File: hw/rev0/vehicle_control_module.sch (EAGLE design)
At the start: 455 parts, among them IC1 SJA1105TELY, IC10 TJA1100HNZ, IC11 KSZ8061MNXI-TR, IC12 TJA1100HNZ, IC14 NUP2202W1T2G, IC15 TLE9252VSKXUMA1, IC16 NUP2202W1T2G, IC17 LP5907QMFX-3.3Q1, IC2 ATSAMV71Q21B-AABT, IC3 TJA1100HNZ, IC4 FT2232HL, IC5 TRS3232EQPWRQ1, IC6 SST26VF032BT-104I_SM, IC7 DS3231SN#, IC8 TLE9252VSKXUMA1, IC9 TPS62242DRVR, J10 5-2337992-3, J11 2301843-1, J12 1017505, J13 2301843-1, J15 693022010811, J2 2305018-2, J27 2041119-2, J3 1017505, J4 1017505, J5 1017505, J6 1017505, J7 1017505, J8 1017505, J9 1017505, U1 122-2920-GR, U2 LM63625, U3 TPS62007-Q1_DGS_10, Y1 NX3225SA-25MHZ-EXS00A-CS11338, Y2 NX2016SA-25.000M-STD-CZS-1, Y3 ABM8AIG-12.000MHZ-1Z-T

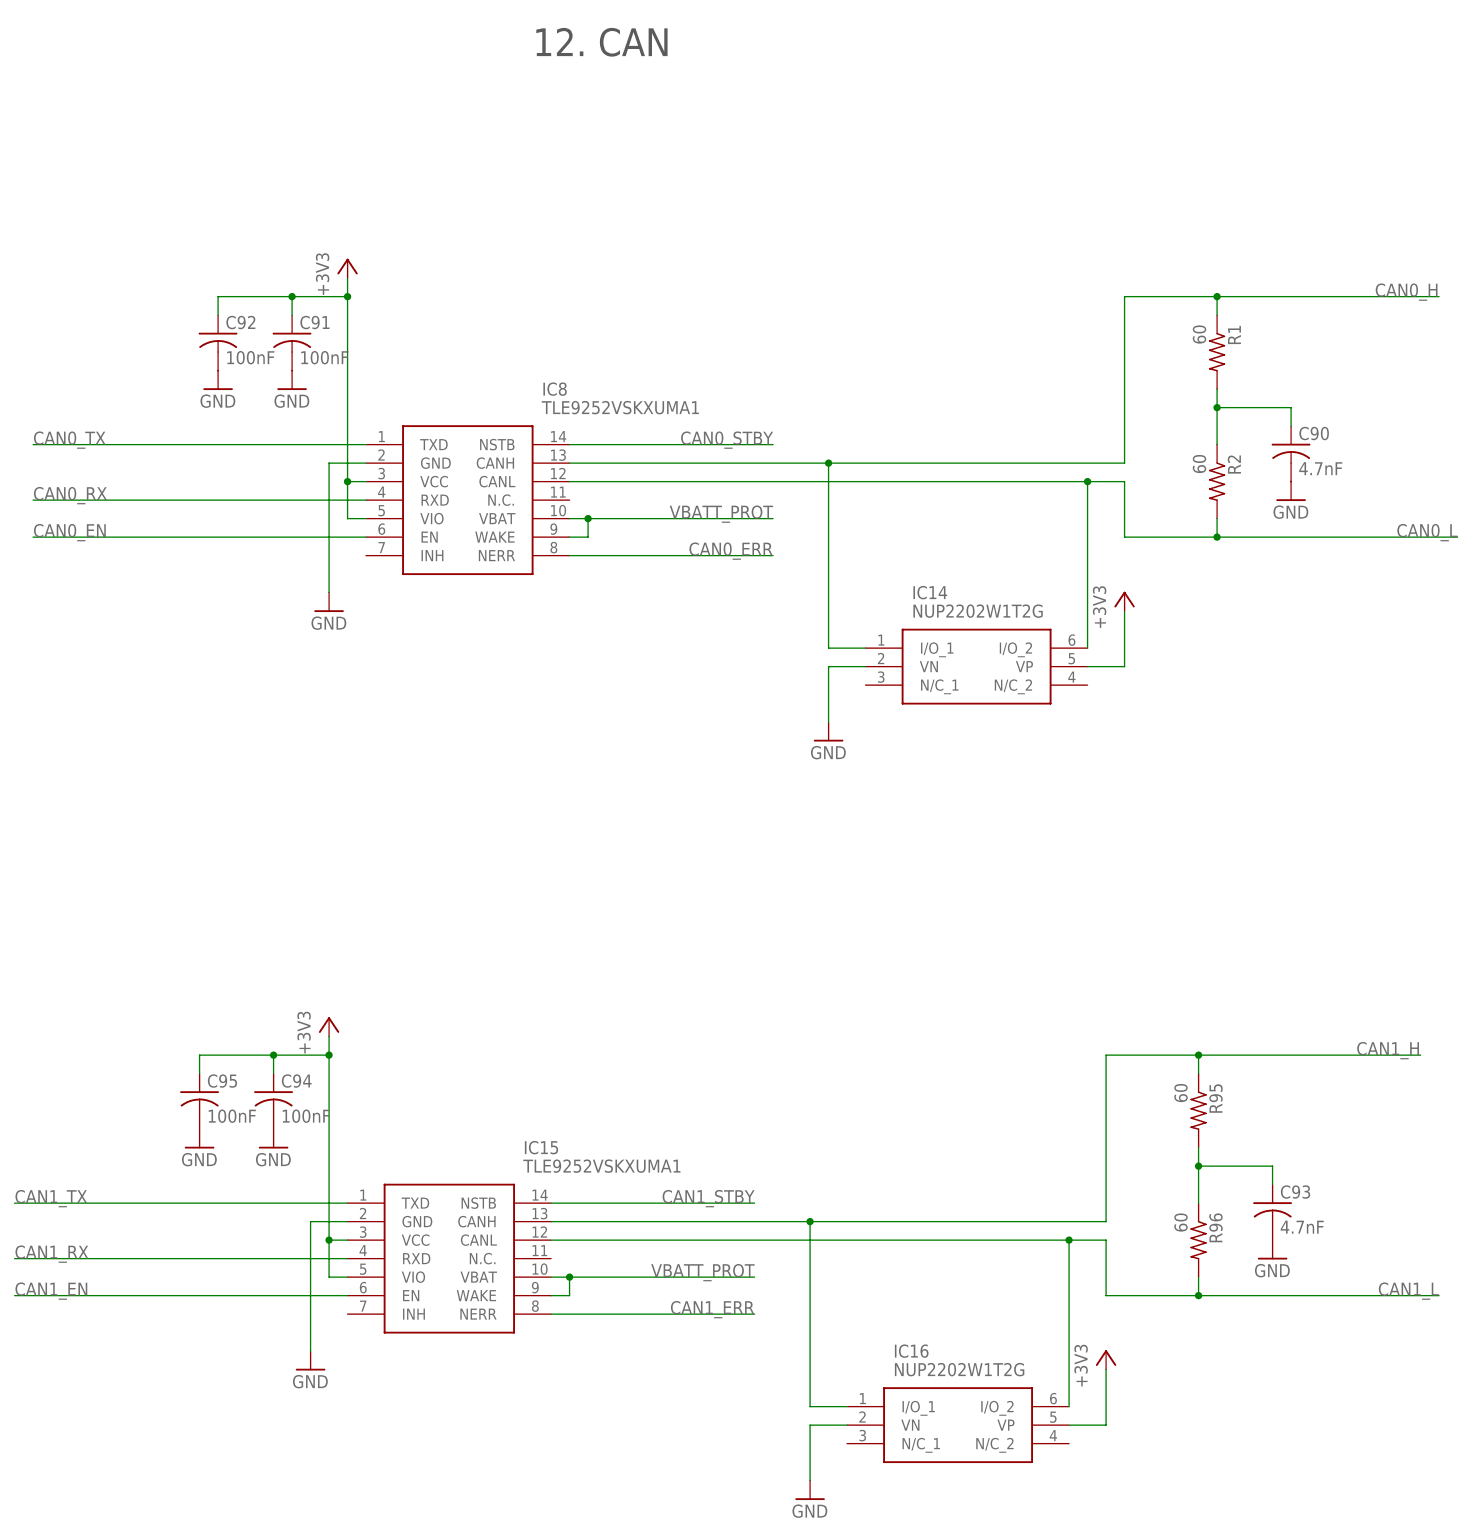
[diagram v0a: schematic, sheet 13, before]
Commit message: Swap to simple CAN transciever, no wake on CAN functionality required
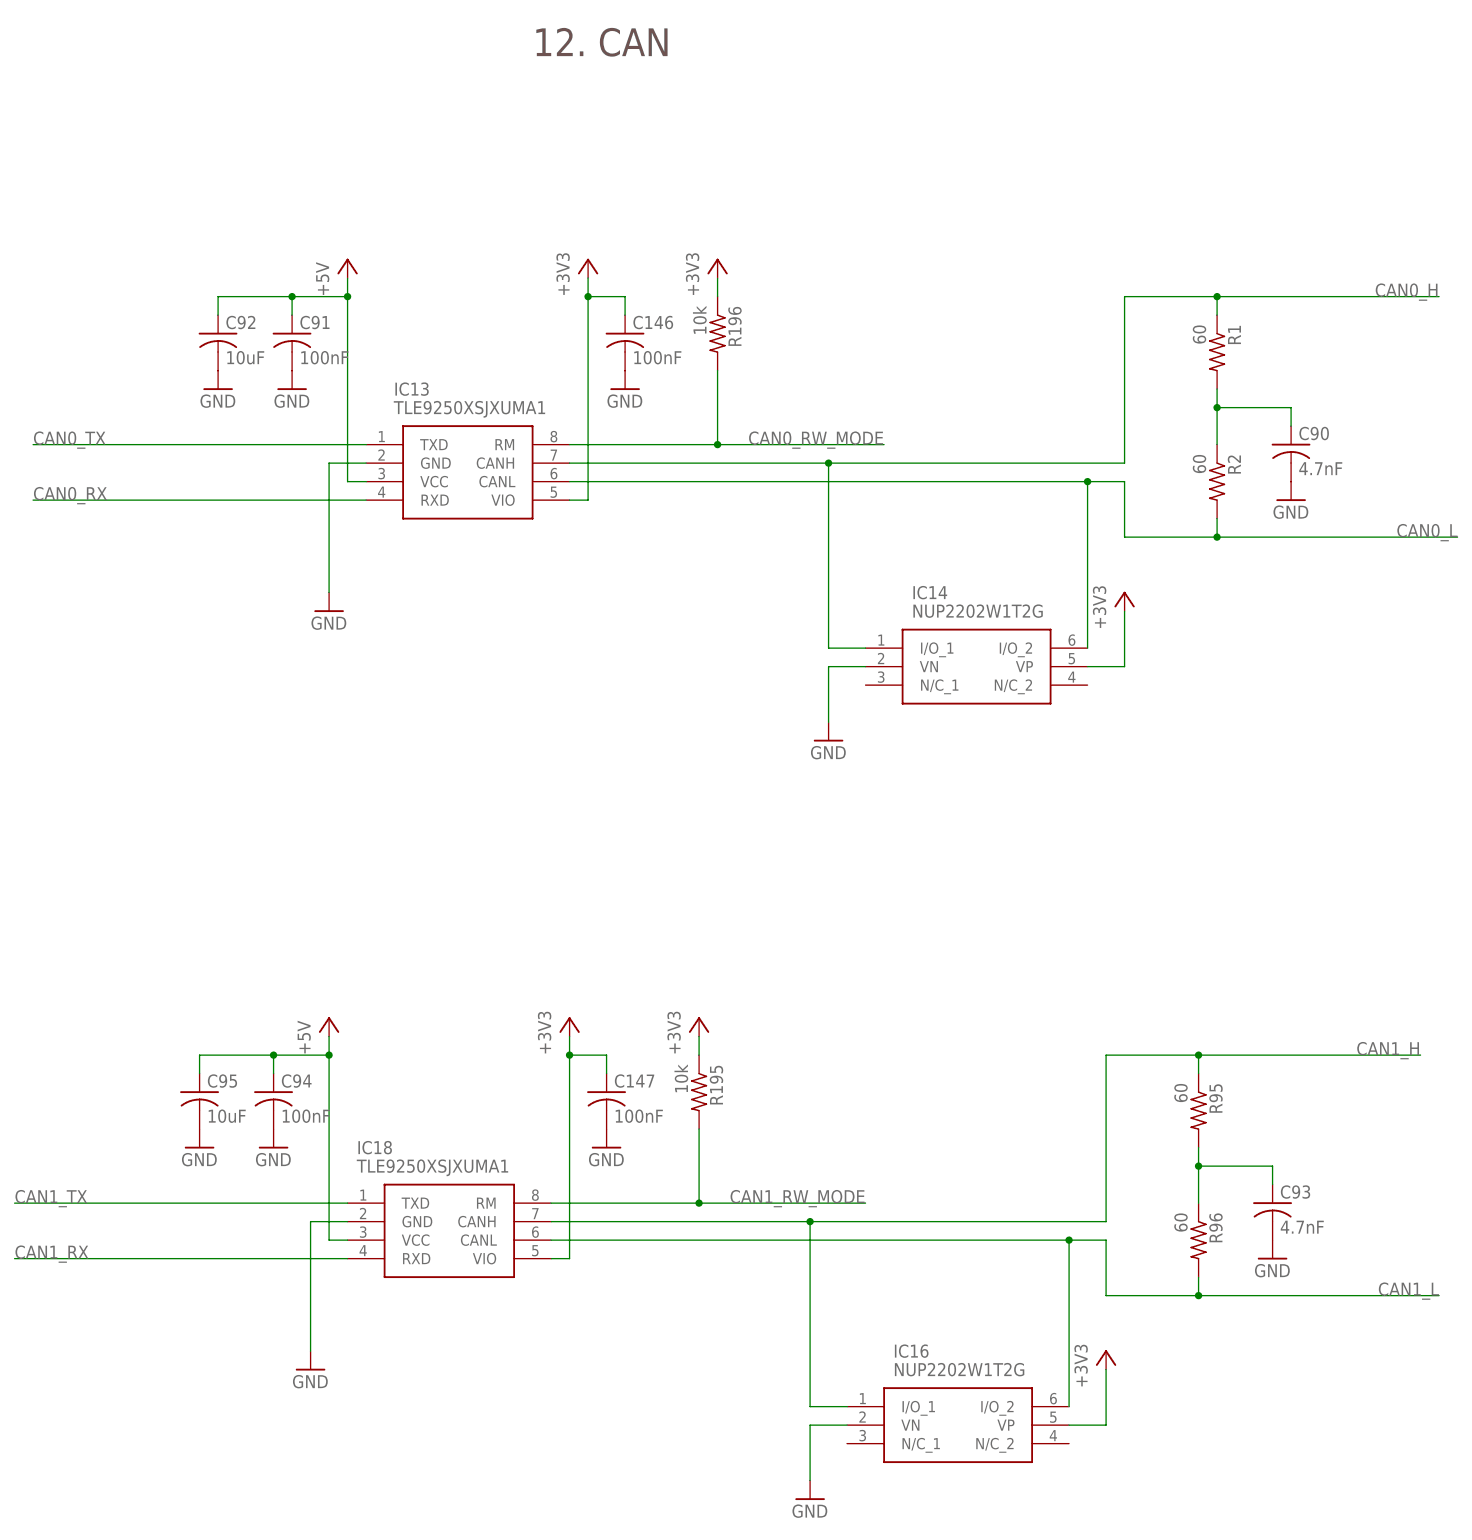
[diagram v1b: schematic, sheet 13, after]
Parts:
- removed IC15, IC8: TLE9252VSKXUMA1, samacsys:TLE9252VSKXUMA1
- added C146, C147: 100nF, rcl:C-USC0603
- added IC13, IC18: TLE9250XSJXUMA1, samacsys:TLE9250XSJXUMA1
- added R195, R196: 10k, rcl:R-US_R0603
- C92, C95: value 100nF -> 10uF
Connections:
- removed net CAN0_EN: IC2.PA22, IC8.EN
- removed net CAN0_ERR: IC2.PC2, IC8.NERR
- removed net CAN0_STBY: IC2.PC1, IC8.NSTB
- removed net CAN1_EN: IC15.EN, IC2.PC11
- removed net CAN1_ERR: IC15.NERR, IC2.PC10
- removed net CAN1_STBY: IC15.NSTB, IC2.PA2
- new net CAN0_RW_MODE: IC13.RM, IC2.PA7, R196.2
- new net CAN1_RW_MODE: IC18.RM, IC2.PA2, R195.2
- net +3V3: now also C146.1, C147.1, IC13.VIO, IC18.VIO, R195.1, R196.1; no longer C91.1, C92.1, C94.1, C95.1, IC15.VCC, IC15.VIO, IC8.VCC, IC8.VIO
- net +5V: now also C91.1, C92.1, C94.1, C95.1, IC13.VCC, IC18.VCC
- net CAN0_H: now also IC13.CANH; no longer IC8.CANH
- net CAN0_L: now also IC13.CANL; no longer IC8.CANL
- net CAN0_RX: now also IC13.RXD; no longer IC8.RXD
- net CAN0_TX: now also IC13.TXD; no longer IC8.TXD
- net CAN1_H: now also IC18.CANH; no longer IC15.CANH
- net CAN1_L: now also IC18.CANL; no longer IC15.CANL
- net CAN1_RX: now also IC18.RXD; no longer IC15.RXD
- net CAN1_TX: now also IC18.TXD; no longer IC15.TXD
- net GND: now also C146.2, C147.2, IC13.GND, IC18.GND; no longer IC15.GND, IC8.GND
- net VBATT_PROT: no longer IC15.VBAT, IC15.WAKE, IC8.VBAT, IC8.WAKE

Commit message: Add digital inputs, connect MCU power supply
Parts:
- removed C30, C31: 8pF, rcl:C-USC0603
- removed IC14, IC16: NUP2202W1T2G, samacsys:NUP2202W1T2G
- removed R183, R188, R193: 1k, rcl:R-US_R0603
- removed Y2: NX2016SA-25.000M-STD-CZS-1, samacsys:NX2016SA-25.000M-STD-CZS-1
- added C148, C149, C150, C151, C152, C153, C154, C155: 0.01uF, rcl:C-USC0603
- added C156, C157, C158, C159, C160, C161, C163, C164, C166, C167, C168, C169, C170, C171, C172: 100nF, rcl:C-USC0603
- added C162: 1uF, rcl:C-USC0603
- added C165: 4.7uF, rcl:C-USC0603
- added D28, D29, D30, D31, D32, D33, D34, D35: BAT54SWFILMY, samacsys:BAT54SWFILMY
- added IC8: 74HC7541D-Q100J, samacsys:74HC7541D-Q100J
- added R198: 4.7k, rcl:R-US_R0603
- R109, R118, R128, R138, R148, R158, R168, R178: value 1k -> 100k
- R113, R123, R133, R143, R153, R163, R173: value 1k -> 4.7k
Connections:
- removed net N$22: C31.1, IC11.XI, Y2.CRYSTAL_2
- removed net N$23: C30.1, IC11.XO, Y2.CRYSTAL_1
- new net EXT_DINPUT_0: R198.1
- new net EXT_DINPUT_1: R113.1
- new net EXT_DINPUT_2: R123.1
- new net EXT_DINPUT_3: R133.1
- new net EXT_DINPUT_4: R143.1
- new net EXT_DINPUT_5: R153.1
- new net EXT_DINPUT_6: R163.1
- new net EXT_DINPUT_7: R173.1
- new net INTREG_1V2: C156.1, C157.1, C158.1, C159.1, C160.1, C161.1, C162.1, C163.1, C164.1, IC2.VDDCORE_1, IC2.VDDCORE_2, IC2.VDDCORE_3, IC2.VDDCORE_4, IC2.VDDCORE_5, IC2.VDDOUT, IC2.VDDPLL, IC2.VDDUTMIC
- new net N$148: C148.1, D29.A,K, IC8.A1, R113.2, R118.2
- new net N$149: C149.1, D30.A,K, IC8.A2, R123.2, R128.2
- new net N$150: C150.1, D31.A,K, IC8.A3, R133.2, R138.2
- new net N$151: C151.1, D28.A,K, IC8.A0, R109.2, R198.2
- new net N$152: C152.1, D32.A,K, IC8.A4, R143.2, R148.2
- new net N$153: C153.1, D33.A,K, IC8.A5, R153.2, R158.2
- new net N$154: C154.1, D34.A,K, IC8.A6, R163.2, R168.2
- new net N$155: C155.1, D35.A,K, IC8.A7, R173.2, R178.2
- new net PROT_DINPUT_0: IC2.PD29, IC8.Y0
- new net PROT_DINPUT_1: IC2.PD15, IC8.Y1
- new net PROT_DINPUT_2: IC2.PC17, IC8.Y2
- new net PROT_DINPUT_3: IC2.PD10, IC8.Y3
- new net PROT_DINPUT_4: IC2.PC16, IC8.Y4
- new net PROT_DINPUT_5: IC2.PA1, IC8.Y5
- new net PROT_DINPUT_6: IC2.PC14, IC8.Y6
- new net PROT_DINPUT_7: IC2.PC11, IC8.Y7
- new net SWITCH_REF_CLK: IC1.CLK_OUT, IC11.XI
- net +3V3: now also C165.1, C166.1, C167.1, C168.1, C169.1, C170.1, C171.1, C172.1, D28.A, D29.A, D30.A, D31.A, D32.A, D33.A, D34.A, D35.A, IC1.VDDIO_CLO, IC1.VDDIO_HOST, IC1.VDDIO_MII0_1, IC1.VDDIO_MII0_2, IC1.VDDIO_MII0_3, IC1.VDDIO_MII1_1, IC1.VDDIO_MII1_2, IC1.VDDIO_MII1_3, IC1.VDDIO_MII2_1, IC1.VDDIO_MII2_2, IC1.VDDIO_MII2_3, IC1.VDDIO_MII3_1, IC1.VDDIO_MII3_3, IC1.VDDIO_MII4_1, IC1.VDDIO_MII4_2, IC1.VDDIO_MII4_3, IC2.VDDIN, IC2.VDDIO_1, IC2.VDDIO_2, IC2.VDDIO_3, IC2.VDDIO_4, IC2.VDDIO_5, IC2.VDDPLL_USB, IC2.VDDUTMII, IC8.VCC; no longer IC14.VP, IC16.VP
- net 3V3_AD_REF: now also IC2.VREFP
- net CAN0_H: no longer IC14.I/O_1
- net CAN0_L: no longer IC14.I/O_2
- net CAN0_RW_MODE: now also IC2.PA22; no longer IC2.PA7
- net CAN1_H: no longer IC16.I/O_1
- net CAN1_L: no longer IC16.I/O_2
- net CAN1_RW_MODE: now also IC2.PC10; no longer IC2.PA2
- net GND: now also C148.2, C149.2, C150.2, C151.2, C152.2, C153.2, C154.2, C155.2, C156.2, C157.2, C158.2, C159.2, C160.2, C161.2, C162.2, C163.2, C164.2, C165.2, C166.2, C167.2, C168.2, C169.2, C170.2, C171.2, C172.2, D28.K, D29.K, D30.K, D31.K, D32.K, D33.K, D34.K, D35.K, IC1.VSSA_OSC, IC1.VSSA_PLL, IC1.VSS_43, IC1.VSS_44, IC2.VREFN, IC8.!OE1, IC8.!OE2, IC8.GND, R109.1, R118.1, R128.1, R138.1, R148.1, R158.1, R168.1, R178.1; no longer C112.2, C113.2, C115.2, C117.2, C119.2, C121.2, C123.2, C125.2, C127.2, C129.2, C131.2, C133.2, C135.2, C137.2, C139.2, C141.2, C143.2, C145.2, C30.2, C31.2, IC14.VN, IC16.VN, R109.2, R113.2, R118.2, R123.2, R128.2, R133.2, R138.2, R143.2, R148.2, R153.2, R158.2, R163.2, R168.2, R173.2, R178.2, R183.2, R188.2, R193.2, Y2.GND_1, Y2.GND_2
- net HIGHSIDE_0_EN: now also IC2.PD11
- net HIGHSIDE_10_EN: now also IC2.PC2
- net HIGHSIDE_11_EN: now also IC2.PC3
- net HIGHSIDE_12_EN: now also IC2.PA16
- net HIGHSIDE_13_EN: now also IC2.PD27
- net HIGHSIDE_14_EN: now also IC2.PC7
- net HIGHSIDE_15_EN: now also IC2.PA15
- net HIGHSIDE_16_EN: now also IC2.PC6
- net HIGHSIDE_17_EN: now also IC2.PD24
- net HIGHSIDE_1_EN: now also IC2.PA2
- net HIGHSIDE_2_EN: now also IC2.PA25
- net HIGHSIDE_3_EN: now also IC2.PA7
- net HIGHSIDE_4_EN: now also IC2.PA31
- net HIGHSIDE_5_EN: now also IC2.PA8
- net HIGHSIDE_6_EN: now also IC2.PA23
- net HIGHSIDE_7_EN: now also IC2.PE1
- net HIGHSIDE_8_EN: now also IC2.PE2
- net HIGHSIDE_9_EN: now also IC2.PC1
- net N$100: now also C115.2
- net N$102: no longer R118.1
- net N$103: now also C117.2
- net N$105: no longer R123.1
- net N$106: now also C119.2
- net N$108: no longer R128.1
- net N$109: now also C121.2
- net N$111: no longer R133.1
- net N$112: now also C123.2
- net N$114: no longer R138.1
- net N$115: now also C125.2
- net N$117: no longer R143.1
- net N$118: now also C127.2
- net N$120: no longer R148.1
- net N$121: now also C129.2
- net N$123: no longer R153.1
- net N$124: now also C131.2
- net N$126: no longer R158.1
- net N$127: now also C133.2
- net N$129: no longer R163.1
- net N$130: now also C135.2
- net N$132: no longer R168.1
- net N$133: now also C137.2
- net N$135: no longer R173.1
- net N$136: now also C139.2
- net N$138: no longer R178.1
- net N$139: now also C141.2
- net N$141: no longer R183.1
- net N$142: now also C143.2
- net N$144: no longer R188.1
- net N$145: now also C145.2
- net N$147: no longer R193.1
- net N$94: now also C112.2
- net N$96: now also C113.2
- net N$97: no longer R109.1
- net N$99: no longer R113.1
- net VDD: now also IC1.VDDA_OSC, IC1.VDDA_PLL, IC1.VDD_CORE_1, IC1.VDD_CORE_2, IC1.VDD_CORE_3, IC1.VDD_CORE_4, IC1.VDD_CORE_5, IC1.VDD_CORE_6, IC1.VDD_CORE_7, IC1.VDD_CORE_8
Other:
- note added: "14. Digital Input"
- note added: "14. Digital Inputs"
- note added: "15. Connectors"
- note removed: "14. Connectors"
